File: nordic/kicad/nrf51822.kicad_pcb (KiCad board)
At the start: 2 copper layers, 0 parts

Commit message: PCB completo
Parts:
- added BT1: Battery, nrf51822:cr2032_bat_holder, B.Cu at (116.8, 119.4)
- added C1: C_Small, Capacitors_SMD:C_0402, F.Cu at (132.6, 111.8)
- added C10: C_Small, Capacitors_SMD:C_0402, F.Cu at (134.6, 130.9)
- added C11: C_Small, Capacitors_SMD:C_0402, F.Cu at (125.3, 126.5)
- added C2: C_Small, Capacitors_SMD:C_0402, F.Cu at (128.8, 111.8)
- added C7: C_Small, Capacitors_SMD:C_0402, F.Cu at (125.2, 129.5)
- added C8: C_Small, Capacitors_SMD:C_0402, F.Cu at (128.8, 121.9)
- added C88: C_Small, Capacitors_SMD:C_0402, F.Cu at (135.1, 128.9)
- added C9: C_Small, Capacitors_SMD:C_0402, F.Cu at (135.0, 124.1)
- added P1: CONN_01X04, Pin_Headers:Pin_Header_Straight_1x04_Pitch2.00mm, F.Cu at (130.3, 135.9)
- added U1: BALF-NRF01E3, BALF-NRF01E3:LGA6S60X50P2X3_100X150X48, F.Cu at (137.9, 126.7)
- added X1: Crystal, Crystals:Crystal_SMD_5032-2pin_5.0x3.2mm, F.Cu at (130.4, 117.6)
- added nRF51822: nRF51822, nrf51822:nRF51822, F.Cu at (129.8, 127.1)
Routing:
- net GND: track 0.00 -> 69.0 mm, vias 0 -> 2
- net VCC: track 0.00 -> 30.5 mm
- net (no net): track 0.00 -> 23.4 mm
- net Net-(C2-Pad2): track 0.00 -> 14.0 mm
- net Net-(C1-Pad2): track 0.00 -> 13.1 mm
- net Net-(P1-Pad2): track 0.00 -> 7.34 mm
- net Net-(P1-Pad1): track 0.00 -> 6.68 mm
- net Net-(C88-Pad1): track 0.00 -> 6.49 mm
- net Net-(U1-Pad4): track 0.00 -> 4.91 mm
- net Net-(U1-Pad3): track 0.00 -> 4.90 mm
- net Net-(C10-Pad1): track 0.00 -> 4.00 mm
- net Net-(C8-Pad1): track 0.00 -> 3.37 mm
- added copper zone on B.Cu, net GND
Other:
- board outline added: 36.8 x 39.4 mm
- net class Default: trace_width 0.25 -> 0.15
- rule trace_min: 0.2 -> 0.0254

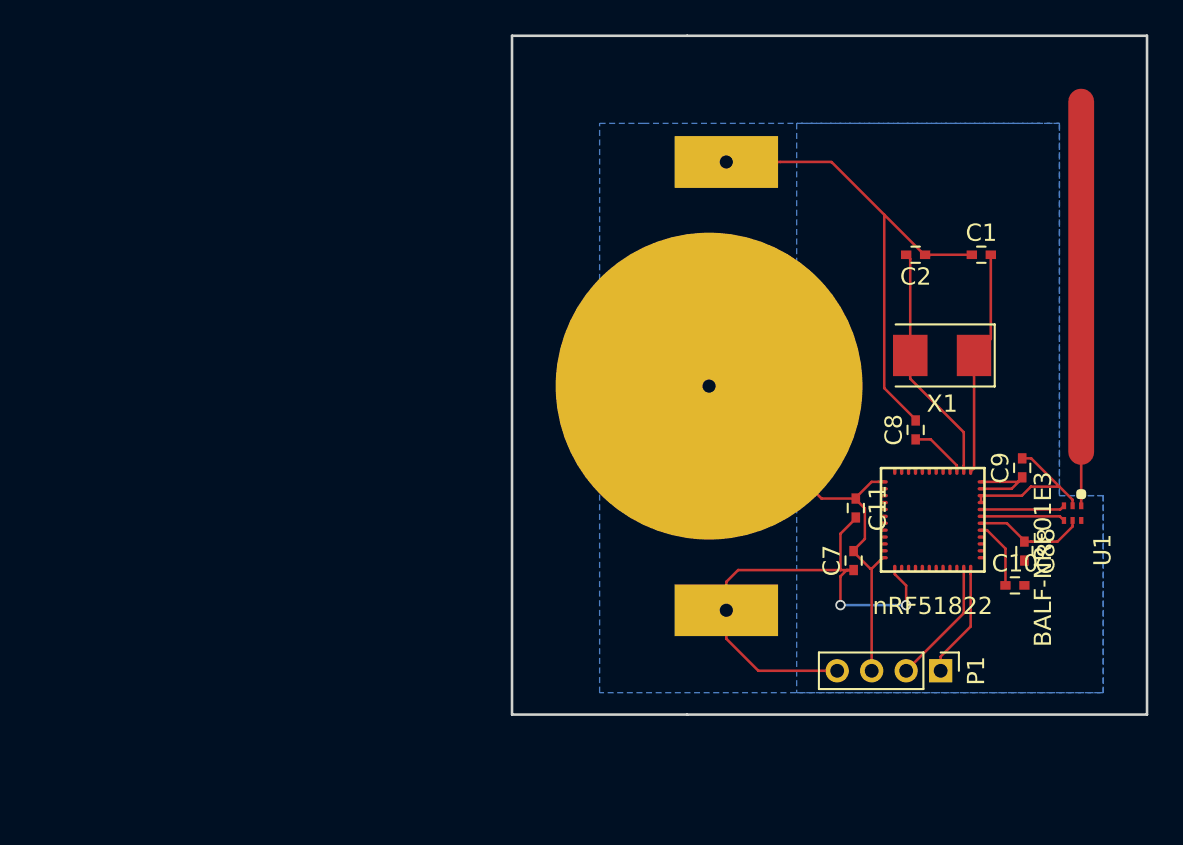
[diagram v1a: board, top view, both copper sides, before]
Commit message: Visual Changes and new Battery pad
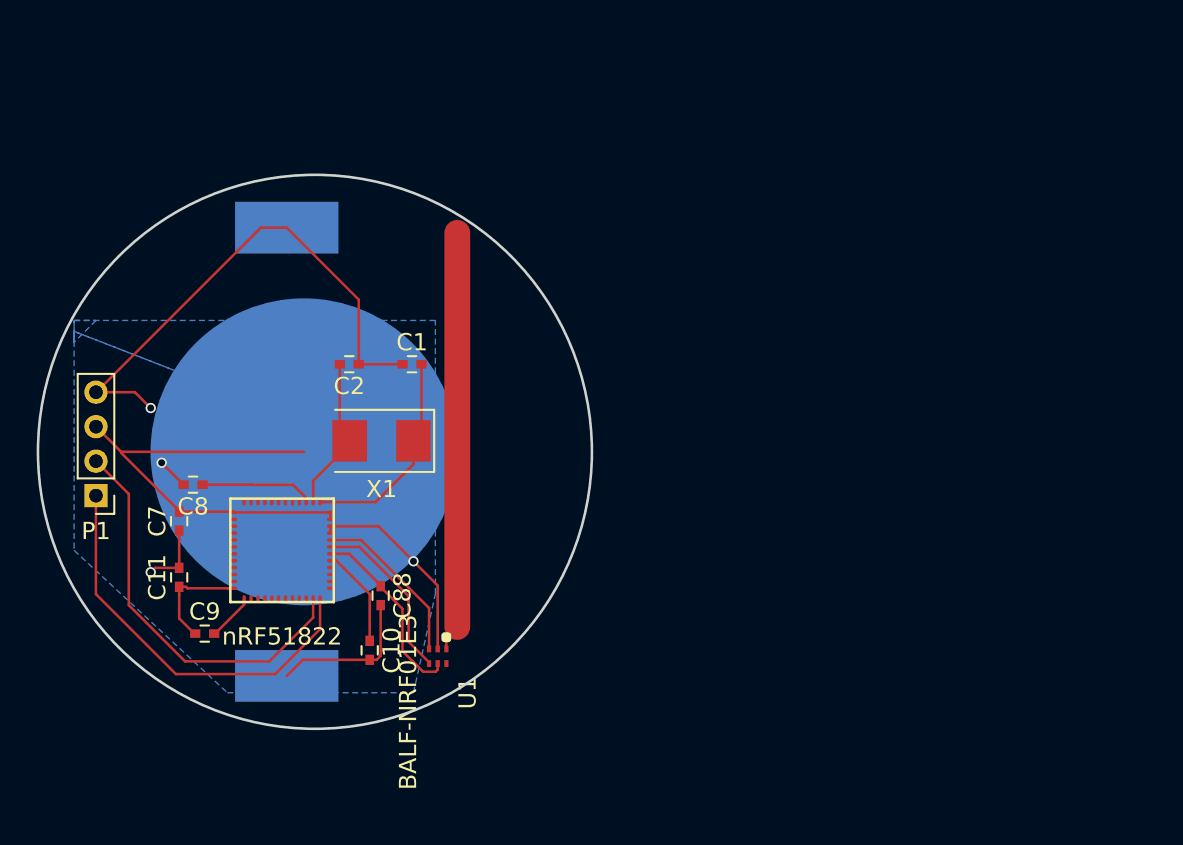
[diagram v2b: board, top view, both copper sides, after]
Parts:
- moved P1 50.0 mm to (81.3, 125.7), turned to 180 degrees
- moved C9 48.4 mm to (87.6, 133.7), turned to 0 degrees
- moved C8 42.0 mm to (86.9, 125.1), turned to 180 degrees
- moved C11 39.4 mm to (86.1, 130.5), turned to 90 degrees
- moved C7 39.2 mm to (86.1, 127.2)
- moved nRF51822 37.8 mm to (92.1, 128.9)
- moved U1 37.7 mm to (101.1, 135.0)
- moved C10 37.6 mm to (97.2, 134.7), turned to 270 degrees
- moved C88 37.4 mm to (97.8, 131.5)
- moved C1 33.6 mm to (99.6, 118.1)
- moved C2 33.5 mm to (96.0, 118.1)
- moved X1 32.9 mm to (97.8, 122.6)
- moved BT1 23.8 mm to (93.3, 123.2), turned to 90 degrees
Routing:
- net Net-(P1-Pad1): track 6.68 -> 23.5 mm
- net Net-(P1-Pad2): track 7.34 -> 23.3 mm
- net GND: track 69.0 -> 59.8 mm, vias 2 -> 3
- net Net-(U1-Pad4): track 4.91 -> 10.1 mm
- net Net-(C2-Pad2): track 14.0 -> 9.11 mm
- net Net-(U1-Pad3): track 4.90 -> 9.73 mm
- net Net-(C88-Pad1): track 6.49 -> 11.0 mm
- net Net-(C8-Pad1): track 3.37 -> 6.57 mm
- net VCC: track 30.5 -> 33.1 mm, vias 0 -> 1
- net Net-(C10-Pad1): track 4.00 -> 5.80 mm
- net (no net): track 23.4 -> 24.4 mm
- net Net-(C1-Pad2): track 13.1 -> 12.3 mm
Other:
- board size 36.8 x 39.4 mm -> 32.1 x 32.1 mm

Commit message: Adicionado Mounting Holes.
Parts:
- added REF**: MountingHole_2.2mm_M2_ISO14580, Pin-Beacon:MountingHole_2.2mm_M2_ISO14580, F.Cu at (106.5, 129.5)
- added REF**: MountingHole_2.2mm_M2_ISO14580, Pin-Beacon:MountingHole_2.2mm_M2_ISO14580, F.Cu at (83.8, 113.8)
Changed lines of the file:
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@@
 (kicad_pcb (version 4) (host pcbnew 4.0.5)
   (general
-    (links 34)
+    (links 0)
     (no_connects 7)
     (area 77.840628 107.050628 110.119372 139.329372)
@@
     (tracks 99)
     (zones 0)
-    (modules 13)
+    (modules 15)
     (nets 12)
   )
@@
     )
   )
+  (module Pin-Beacon:MountingHole_2.2mm_M2_ISO14580 (layer F.Cu)
+    (at 106.5 129.5)
+    (descr "Mounting Hole 2.2mm, no annular, M2, ISO14580")
+    (tags "mounting hole 2.2mm no annular m2 iso14580")
+    (fp_text reference REF** (at 0 -2) (layer F.SilkS)
+      (effects (font (size 1 1) (thickness 0.15)))
+    )
+    (fp_text value MountingHole_2.2mm_M2_ISO14580 (at 0 2.9) (layer F.Fab)
+      (effects (font (size 1 1) (thickness 0.15)))
+    )
+    (fp_circle (center 0 0) (end 1.27 0) (layer Cmts.User) (width 0.15))
+    (fp_circle (center 0 0) (end 1.27 0) (layer F.CrtYd) (width 0.05))
+    (pad 1 np_thru_hole circle (at 0 0) (size 2.2 2.2) (drill 2.2) (layers *.Cu *.Mask))
+  )
+  (module Pin-Beacon:MountingHole_2.2mm_M2_ISO14580 (layer F.Cu)
+    (at 83.75 113.75)
+    (descr "Mounting Hole 2.2mm, no annular, M2, ISO14580")
+    (tags "mounting hole 2.2mm no annular m2 iso14580")
+    (fp_text reference REF** (at 1.5 -2) (layer F.SilkS)
+      (effects (font (size 1 1) (thickness 0.15)))
+    )
+    (fp_text value MountingHole_2.2mm_M2_ISO14580 (at 0 2.9) (layer F.Fab)
+      (effects (font (size 1 1) (thickness 0.15)))
+    )
+    (fp_circle (center 0 0) (end 1.27 0) (layer Cmts.User) (width 0.15))
+    (fp_circle (center 0 0) (end 1.27 0) (layer F.CrtYd) (width 0.05))
+    (pad 1 np_thru_hole circle (at 0 0) (size 2.2 2.2) (drill 2.2) (layers *.Cu *.Mask))
+  )
   (gr_circle (center 93.98 123.19) (end 78.74 128.27) (layer Edge.Cuts) (width 0.15))

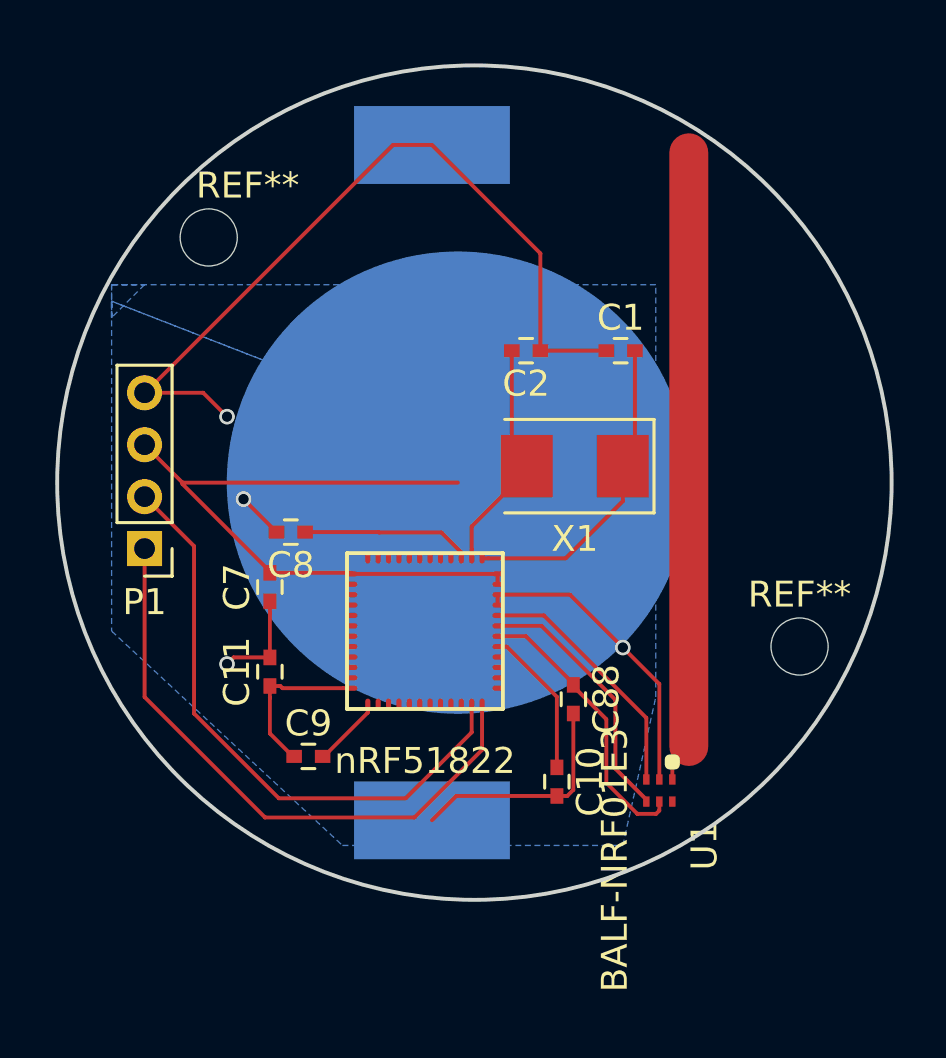
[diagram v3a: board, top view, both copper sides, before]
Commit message: Adicionado pino pra anti-tampering, botão de reset e logo
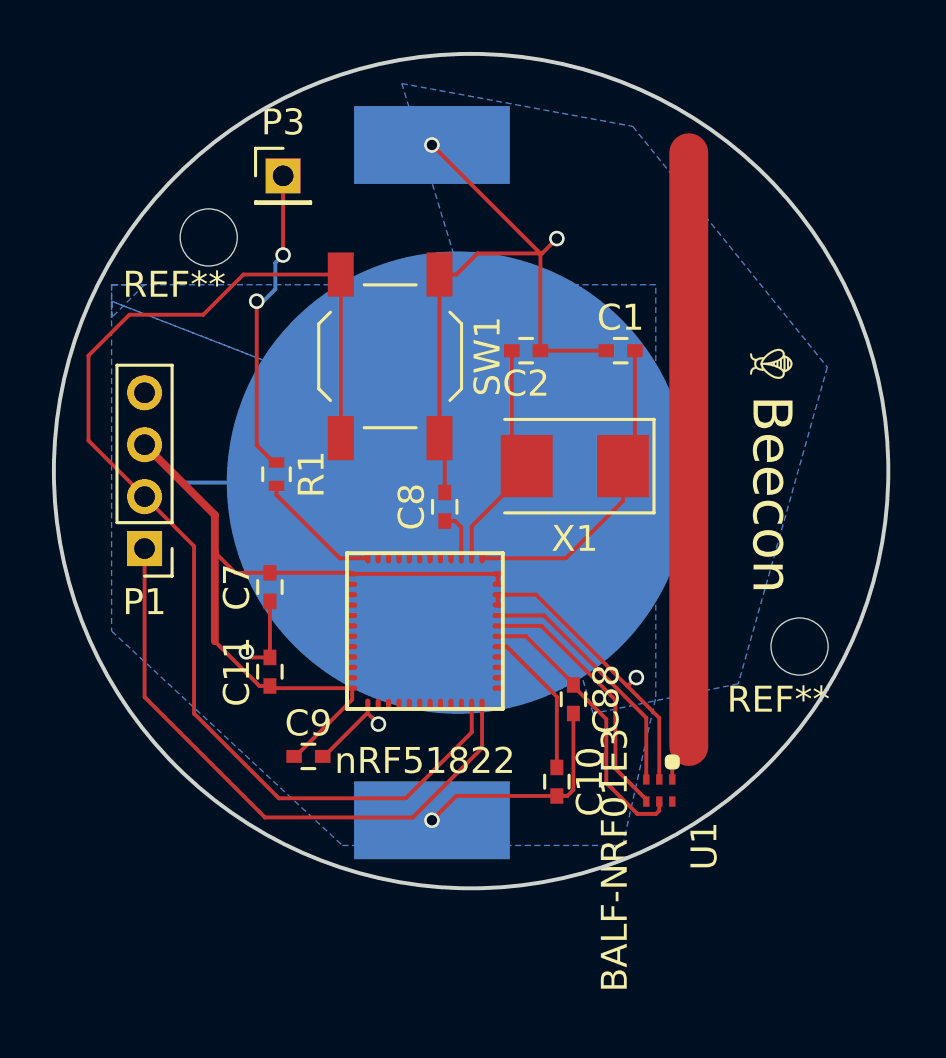
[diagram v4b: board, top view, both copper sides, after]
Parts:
- added G***: LOGO, Pin-Beacon:logo, F.Cu at (105.4, 118.6)
- added P3: CONN_01X01, Pin_Headers:Pin_Header_Straight_1x01_Pitch2.00mm, F.Cu at (86.6, 111.4)
- added R1: R_Small, Resistors_SMD:R_0402, F.Cu at (86.4, 122.9)
- added SW1: SW_Push, Buttons_Switches_SMD:SW_SPST_TL3342, F.Cu at (90.7, 118.3)
- moved C8 6.01 mm to (92.8, 124.1), turned to 90 degrees
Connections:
- U1 pad 1: (no net) -> Net-(AE1-Pad1)
- nRF51822 pad 10: (no net) -> Net-(nRF51822-Pad10)
- nRF51822 pad 11: (no net) -> Net-(nRF51822-Pad11)
- nRF51822 pad 14: (no net) -> Net-(nRF51822-Pad14)
- nRF51822 pad 15: (no net) -> Net-(nRF51822-Pad15)
- nRF51822 pad 16: (no net) -> Net-(nRF51822-Pad16)
- nRF51822 pad 17: (no net) -> Net-(nRF51822-Pad17)
- nRF51822 pad 18: (no net) -> Net-(nRF51822-Pad18)
- nRF51822 pad 19: (no net) -> Net-(nRF51822-Pad19)
- nRF51822 pad 2: (no net) -> Net-(nRF51822-Pad2)
- nRF51822 pad 20: (no net) -> Net-(nRF51822-Pad20)
- nRF51822 pad 21: (no net) -> Net-(nRF51822-Pad21)
- nRF51822 pad 22: (no net) -> Net-(nRF51822-Pad22)
- nRF51822 pad 25: (no net) -> Net-(nRF51822-Pad25)
- nRF51822 pad 26: (no net) -> Net-(nRF51822-Pad26)
- nRF51822 pad 27: (no net) -> Net-(nRF51822-Pad27)
- nRF51822 pad 28: (no net) -> Net-(nRF51822-Pad28)
- nRF51822 pad 3: (no net) -> Net-(nRF51822-Pad3)
- nRF51822 pad 4: (no net) -> Net-(nRF51822-Pad4)
- nRF51822 pad 40: (no net) -> Net-(nRF51822-Pad40)
- nRF51822 pad 41: (no net) -> Net-(nRF51822-Pad41)
- nRF51822 pad 42: (no net) -> Net-(nRF51822-Pad42)
- nRF51822 pad 43: (no net) -> Net-(nRF51822-Pad43)
- nRF51822 pad 44: (no net) -> Net-(nRF51822-Pad44)
- nRF51822 pad 45: (no net) -> Net-(nRF51822-Pad45)
- nRF51822 pad 46: (no net) -> Net-(nRF51822-Pad46)
- nRF51822 pad 47: (no net) -> Net-(nRF51822-Pad47)
- nRF51822 pad 48: (no net) -> Net-(R1-Pad2)
- nRF51822 pad 5: (no net) -> Net-(nRF51822-Pad5)
- nRF51822 pad 6: (no net) -> Net-(nRF51822-Pad6)
- nRF51822 pad 7: (no net) -> Net-(nRF51822-Pad7)
- nRF51822 pad 8: (no net) -> Net-(nRF51822-Pad8)
- nRF51822 pad 9: (no net) -> Net-(nRF51822-Pad9)
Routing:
- net Net-(AE1-Pad1): track 0.00 -> 24.4 mm
- net (no net): track 24.4 -> 0.00 mm
- net Net-(P1-Pad2): track 23.3 -> 47.0 mm
- net Net-(P3-Pad1): track 0.00 -> 12.0 mm, vias 0 -> 2
- net VCC: track 33.1 -> 42.7 mm, vias 1 -> 0
- net GND: track 59.8 -> 52.9 mm, vias 3 -> 6
- net Net-(R1-Pad2): track 0.00 -> 4.87 mm
- net Net-(C8-Pad1): track 6.57 -> 1.93 mm
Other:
- board text added: "Beecon"

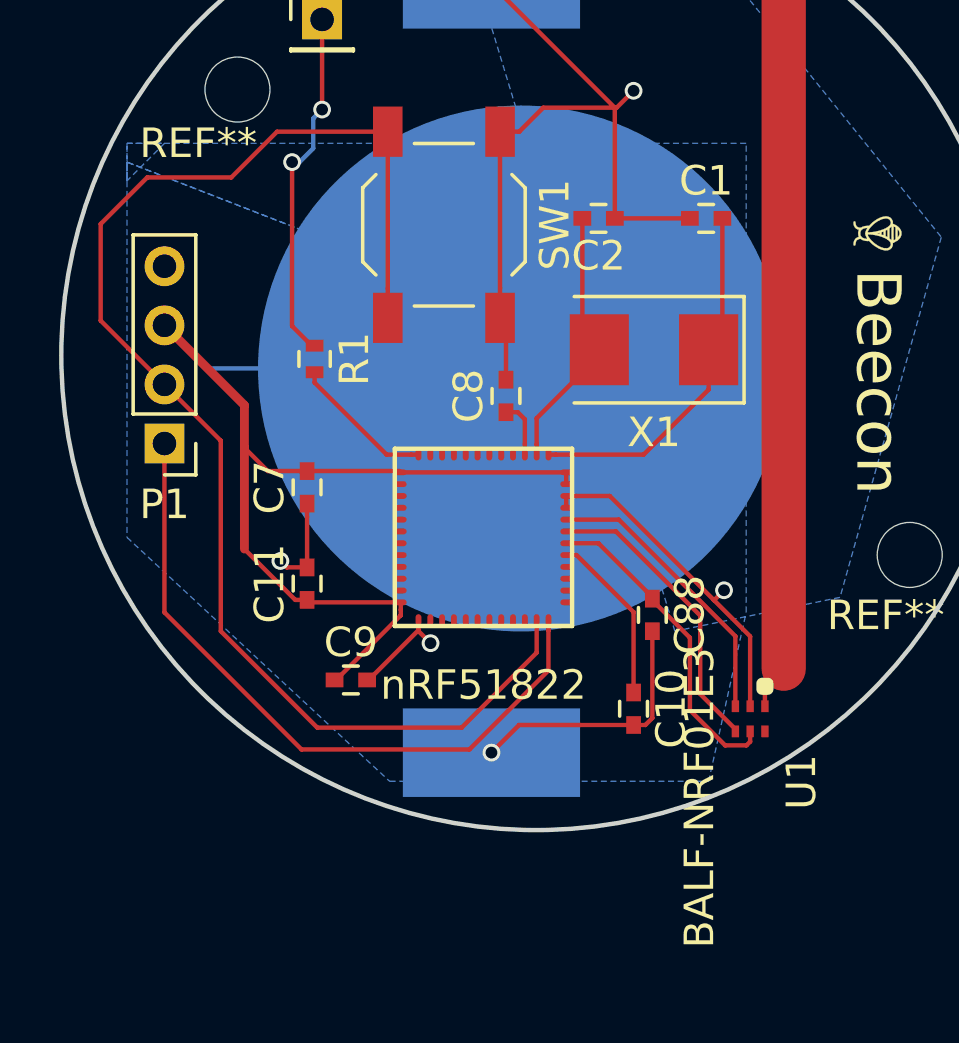
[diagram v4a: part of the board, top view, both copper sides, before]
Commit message: Adicionado componentes 3D
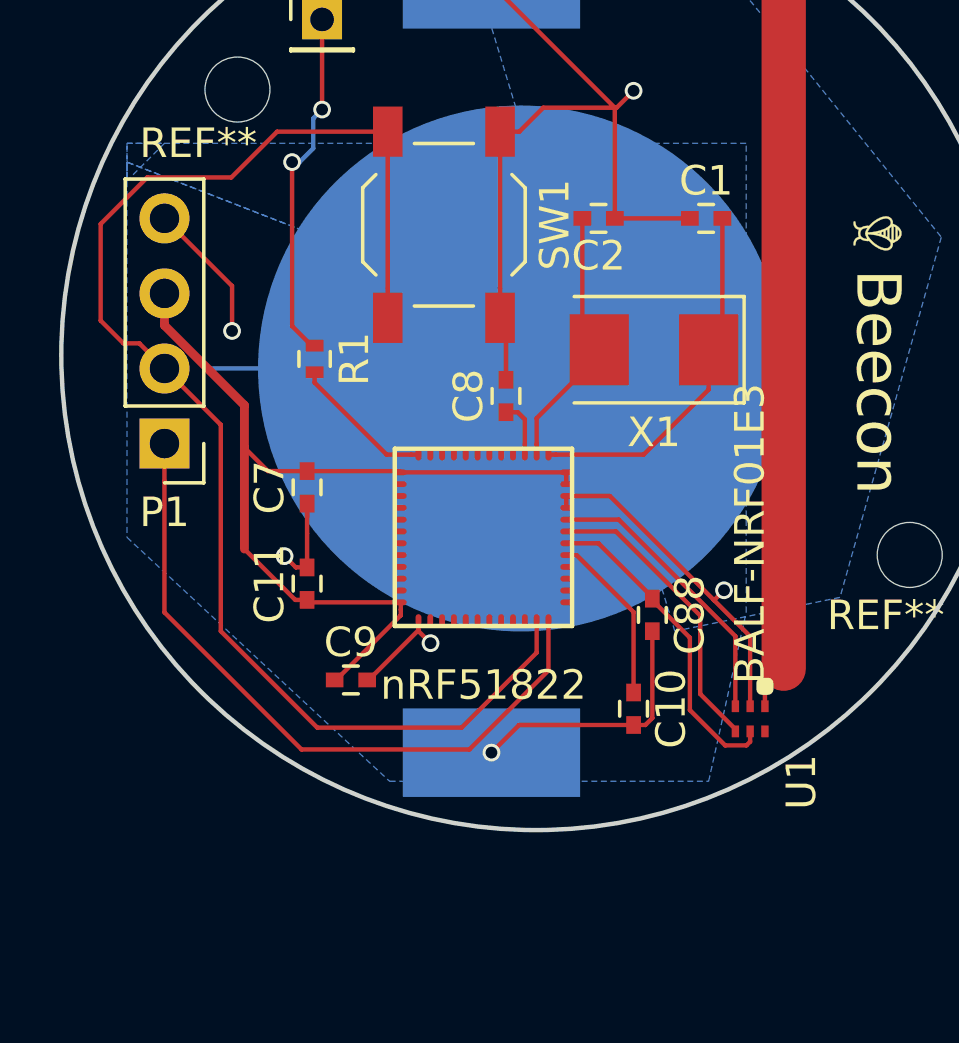
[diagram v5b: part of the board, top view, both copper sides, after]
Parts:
- BT1: footprint nrf51822:cr2032_bat_holder -> Pin-Beacon:cr2032_bat_holder
- P1: footprint Pin_Headers:Pin_Header_Straight_1x04_Pitch2.00mm -> Pin_Headers:Pin_Header_Straight_1x04_Pitch2.54mm
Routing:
- net GND: track 52.9 -> 58.0 mm, vias 6 -> 7
- net VCC: track 42.7 -> 43.7 mm
